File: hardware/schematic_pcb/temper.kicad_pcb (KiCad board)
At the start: 2 copper layers, 36 x 96.5 mm, 48 parts, among them J1 conn_01x03, J2 conn_01x03, J3 conn_01x03, J4 conn_01x03, J5 Charge Connector, J6 MCU Serial I/F, J7 Conn_01x08, M1 DMP3099L-7, Q1 2N7002, SW1 Reset, SW2 Factory Reset, SW3 ON/OFF, U1 MCP9700, U2 ESP32-WROOM-32, U3 APX803-31SAG-7

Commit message: Add 1.5 HW design.
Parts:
- removed MH1, MH2, MH3, MH4: MountingHole_3.2mm_M3, MountingHole:MountingHole_3.2mm_M3
- removed U3: APX803-31SAG-7, Package_TO_SOT_SMD:SOT-23
- added H1: MountingHole_3.2mm_M3, MountingHole:MountingHole_3.2mm_M3, F.Cu at (134.0, 56.8)
- added H2: MountingHole_3.2mm_M3, MountingHole:MountingHole_3.2mm_M3, F.Cu at (156.0, 56.8)
- added H3: MountingHole_3.2mm_M3, MountingHole:MountingHole_3.2mm_M3, F.Cu at (162.0, 145.2)
- added H4: MountingHole_3.2mm_M3, MountingHole:MountingHole_3.2mm_M3, F.Cu at (134.0, 145.2)
- added JP2: Jumper_2_Bridged, Jumper:SolderJumper-2_P1.3mm_Bridged_RoundedPad1.0x1.5mm, F.Cu at (132.8, 137.3)
- added Q2: 2N7002, Package_TO_SOT_SMD:SOT-23-3, F.Cu at (154.0, 126.9)
- added R17: 100k, Resistor_SMD:R_0402_1005Metric_Pad0.72x0.64mm_HandSolder, F.Cu at (157.8, 126.7)
- C1, C3, C4, C5: footprint Capacitor_SMD:C_0603_1608Metric -> Capacitor_SMD:C_0402_1005Metric_Pad0.74x0.62mm_HandSolder
- C2: value 0.1uf -> DNF; footprint Capacitor_SMD:C_0603_1608Metric -> Capacitor_THT:CP_Radial_D6.3mm_P2.50mm
- C6: value 470uf -> 0.1uf; footprint Capacitor_THT:CP_Radial_D6.3mm_P2.50mm -> Capacitor_SMD:C_0402_1005Metric_Pad0.74x0.62mm_HandSolder
- C7: value 0.1uf -> 22uf; footprint Capacitor_SMD:C_0603_1608Metric -> Capacitor_SMD:C_1206_3216Metric_Pad1.33x1.80mm_HandSolder
- D1: value PWR LED -> Blue Bluetooth LED; footprint LED_SMD:LED_1206_3216Metric -> LED_SMD:LED_0805_2012Metric_Pad1.15x1.40mm_HandSolder
- D2: value Blue Bluetooth LED -> Green WiFi LED; footprint LED_SMD:LED_1206_3216Metric -> LED_SMD:LED_0805_2012Metric_Pad1.15x1.40mm_HandSolder
- D3: value Green WiFi LED -> Red Charging LED; footprint LED_SMD:LED_1206_3216Metric -> LED_SMD:LED_0805_2012Metric_Pad1.15x1.40mm_HandSolder
- D4: value Red Charging LED -> PWR LED; footprint LED_SMD:LED_1206_3216Metric -> LED_SMD:LED_0805_2012Metric_Pad1.15x1.40mm_HandSolder
- J7: value Conn_01x08 -> Conn_01x10; footprint Connector_PinHeader_2.54mm:PinHeader_1x08_P2.54mm_Vertical -> Connector_PinHeader_2.54mm:PinHeader_1x10_P2.54mm_Vertical
- M1: value DMP3099L-7 -> AO3401A
- R1, R14, R2, R3, R4, R5, R8: footprint Resistor_SMD:R_0603_1608Metric_Pad0.98x0.95mm_HandSolder -> Resistor_SMD:R_0402_1005Metric_Pad0.72x0.64mm_HandSolder
- R10: value DNF -> 100k; footprint Resistor_SMD:R_0603_1608Metric_Pad0.98x0.95mm_HandSolder -> Resistor_SMD:R_0402_1005Metric_Pad0.72x0.64mm_HandSolder
- R11: value 150k -> 22k; footprint Resistor_SMD:R_0603_1608Metric_Pad0.98x0.95mm_HandSolder -> Resistor_SMD:R_0402_1005Metric_Pad0.72x0.64mm_HandSolder
- R12: value 47k -> 470R; footprint Resistor_SMD:R_0603_1608Metric_Pad0.98x0.95mm_HandSolder -> Resistor_SMD:R_0402_1005Metric_Pad0.72x0.64mm_HandSolder
- R13: value 470R -> 100k; footprint Resistor_SMD:R_0603_1608Metric_Pad0.98x0.95mm_HandSolder -> Resistor_SMD:R_0402_1005Metric_Pad0.72x0.64mm_HandSolder
- R15: value 150k -> 47k; footprint Resistor_SMD:R_0603_1608Metric_Pad0.98x0.95mm_HandSolder -> Resistor_SMD:R_0402_1005Metric_Pad0.72x0.64mm_HandSolder
- R16: value 68k -> 470R; footprint Resistor_SMD:R_0603_1608Metric_Pad0.98x0.95mm_HandSolder -> Resistor_SMD:R_0402_1005Metric_Pad0.72x0.64mm_HandSolder
- R6: value 470R -> 10k; footprint Resistor_SMD:R_0603_1608Metric_Pad0.98x0.95mm_HandSolder -> Resistor_SMD:R_0402_1005Metric_Pad0.72x0.64mm_HandSolder
- R7: value 10k -> 470R; footprint Resistor_SMD:R_0603_1608Metric_Pad0.98x0.95mm_HandSolder -> Resistor_SMD:R_0402_1005Metric_Pad0.72x0.64mm_HandSolder
- R9: value 470R -> DNF; footprint Resistor_SMD:R_0603_1608Metric_Pad0.98x0.95mm_HandSolder -> Resistor_SMD:R_0402_1005Metric_Pad0.72x0.64mm_HandSolder
- SW1: value Reset -> ON/OFF; footprint PJA_Switches:switch_SPST_5mmx3mmx2.5mm -> Button_Switch_SMD:SW_SPST_SKQG_WithoutStem
- SW2: value Factory Reset -> ON/OFF; footprint PJA_Switches:switch_SPST_5mmx3mmx2.5mm -> Button_Switch_SMD:SW_SPST_SKQG_WithoutStem
- SW3: footprint PJA_Switches:switch_SPST_5mmx3mmx2.5mm -> Button_Switch_SMD:SW_SPST_SKQG_WithoutStem
- moved C3 70.8 mm to (143.2, 139.0)
- moved D4 69.0 mm to (148.0, 133.5), turned to 0 degrees
- moved C7 66.8 mm to (156.4, 63.0), turned to 0 degrees
- moved R4 61.3 mm to (155.2, 66.0), turned to 180 degrees
- moved D1 42.5 mm to (138.7, 92.0), turned to -90 degrees
- moved R16 37.4 mm to (147.5, 131.8), turned to 0 degrees
- moved C4 35.5 mm to (157.9, 66.0), turned to 0 degrees
- moved R9 33.6 mm to (141.2, 101.5), turned to 90 degrees
- moved R8 32.9 mm to (152.2, 62.0), turned to 0 degrees
- moved R12 32.6 mm to (141.0, 65.7), turned to 90 degrees
- moved R6 32.6 mm to (141.2, 98.9), turned to 90 degrees
- moved R13 31.7 mm to (141.2, 96.2)
- moved R15 17.8 mm to (138.8, 111.2), turned to 0 degrees
- moved J7 17.5 mm to (157.5, 91.0)
- moved C1 15.6 mm to (150.5, 126.1), turned to -90 degrees
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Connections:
- net Net-(J7-Pin_5) renamed /PWR_SW_A
- net Net-(J7-Pin_6) renamed /PWR_SW_B
- C2 pad 1: //RESET -> 3v3
- C3 pad 1: 3v3 -> //RESET
- C4 pad 1: Net-(U2-IO34) -> 3v3
- C4 pad 2: Net-(Q1-D) -> GND
- C5 pad 1: Net-(U2-IO35) -> Net-(U2-IO34)
- C6 pad 1: 3v3 -> Net-(U2-IO35)
- C6 pad 2: GND -> Net-(Q1-D)
- D1 pad 2: 3v3 -> Net-(D1-A)
- D3 pad 1: Net-(D3-K) -> /CHRG_STAT
- D4 pad 2: Net-(D4-A) -> 3v3
- J6 pad 2: /TXD -> Net-(J6-Pin_2)
- J7 pad 7: Net-(D4-K) -> /CHRG_STAT
- JP1 pad 2: /TXD -> Net-(J6-Pin_2)
- R10 pad 1: Net-(Q1-D) -> /+VBAT
- R10 pad 2: GND -> Net-(U2-IO34)
- R11 pad 1: /+VBAT -> Net-(U2-IO34)
- R11 pad 2: Net-(U2-IO34) -> Net-(Q1-D)
- R12 pad 1: Net-(U2-IO34) -> /+VBAT
- R12 pad 2: Net-(Q1-D) -> Net-(D3-A)
- R13 pad 1: /+VBAT -> Net-(Q1-G)
- R13 pad 2: Net-(D4-A) -> GND
- R14 pad 1: Net-(Q1-G) -> 3v3
- R14 pad 2: GND -> Net-(U2-IO35)
- R15 pad 1: 3v3 -> Net-(U2-IO35)
- R15 pad 2: Net-(U2-IO35) -> Net-(Q1-D)
- R16 pad 1: Net-(U2-IO35) -> Net-(D4-K)
- R16 pad 2: Net-(Q1-D) -> Net-(Q2-D)
- R6 pad 1: Net-(D1-K) -> 3v3
- R6 pad 2: GND -> Net-(SW2-B)
- R7 pad 1: 3v3 -> Net-(D1-K)
- R7 pad 2: Net-(SW2-B) -> GND
- R9 pad 1: Net-(D3-K) -> Net-(Q1-D)
- U2 pad 24: Net-(D3-A) -> Net-(D2-A)
- U2 pad 26: Net-(D2-A) -> Net-(D1-A)
- U2 pad 33: unconnected-(U2-IO21-Pad33) -> //CHRG_OFF
- U2 pad 36: unconnected-(U2-IO22-Pad36) -> //DIS_PWR_LED
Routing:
- net Net-(D4-K): track 91.4 -> 1.77 mm
- net /CHRG_STAT: track 0.00 -> 57.3 mm, vias 0 -> 1
- net //DIS_PWR_LED: track 0.00 -> 47.1 mm, vias 0 -> 4
- net //CHRG_OFF: track 0.00 -> 41.4 mm, vias 0 -> 2
- net /PWR_SW_B: track 29.1 -> 66.4 mm, vias 1 -> 2
- net Net-(D2-K): track 36.7 -> 1.93 mm, vias 2 -> 0
- net Net-(D3-A): track 36.4 -> 2.29 mm, vias 2 -> 0
- net //RESET: track 79.1 -> 112.0 mm, vias 2 -> 1
- net Net-(J1-Pin_3): track 73.1 -> 103.4 mm
- net Net-(D1-A): track 0.00 -> 22.9 mm, vias 0 -> 4
- net Net-(U2-IO35): track 37.1 -> 59.8 mm
- net Net-(J6-Pin_2): track 0.00 -> 21.8 mm, vias 0 -> 1
- net /PWR_SW_A: track 43.2 -> 63.1 mm, vias 1 -> 0
- net /TXD: track 98.6 -> 80.4 mm, vias 1 -> 4
- net Net-(Q1-G): track 47.9 -> 30.6 mm
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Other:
- board text added: "ON OFF"
- board text added: "TEMPER V1.5 ASY0400V1.5"
- board text removed: "ON / OFF"
- board text removed: "TEMPER V1.4 ASY0400V1.4"

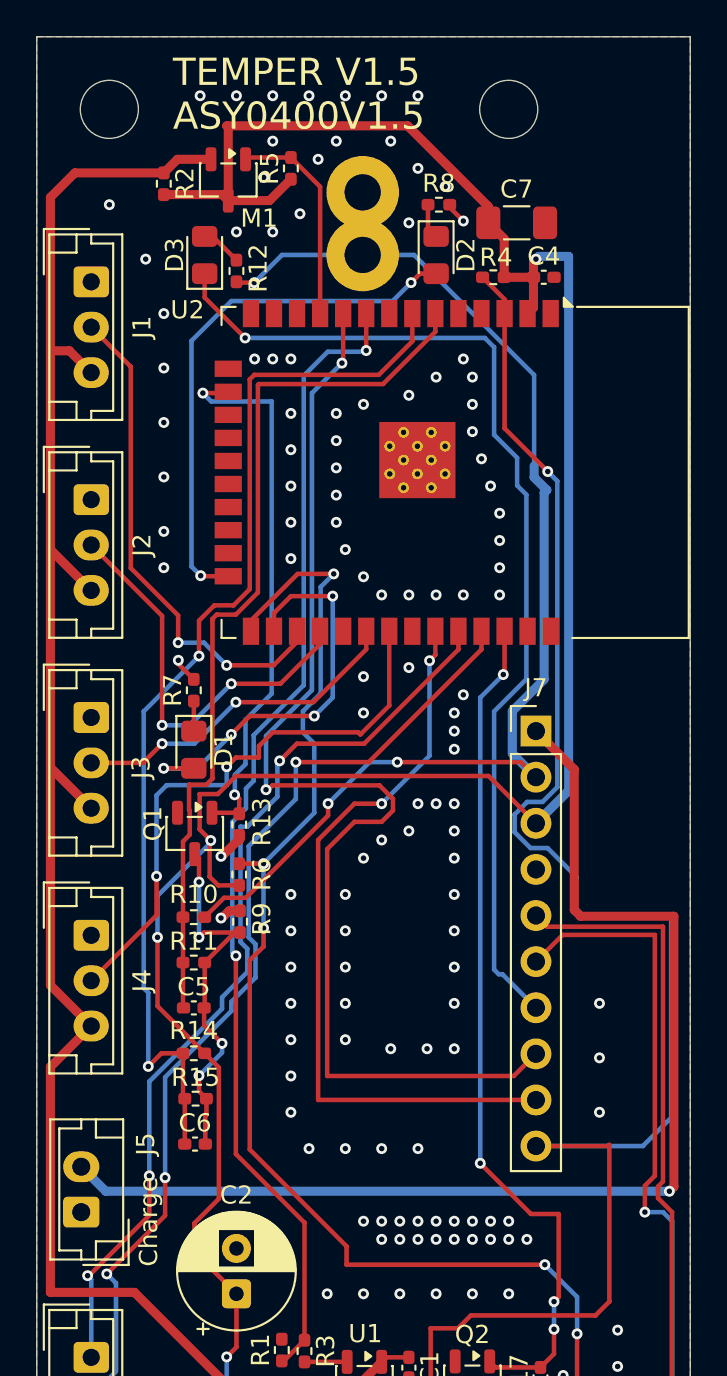
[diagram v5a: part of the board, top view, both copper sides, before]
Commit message: Update to add D5.
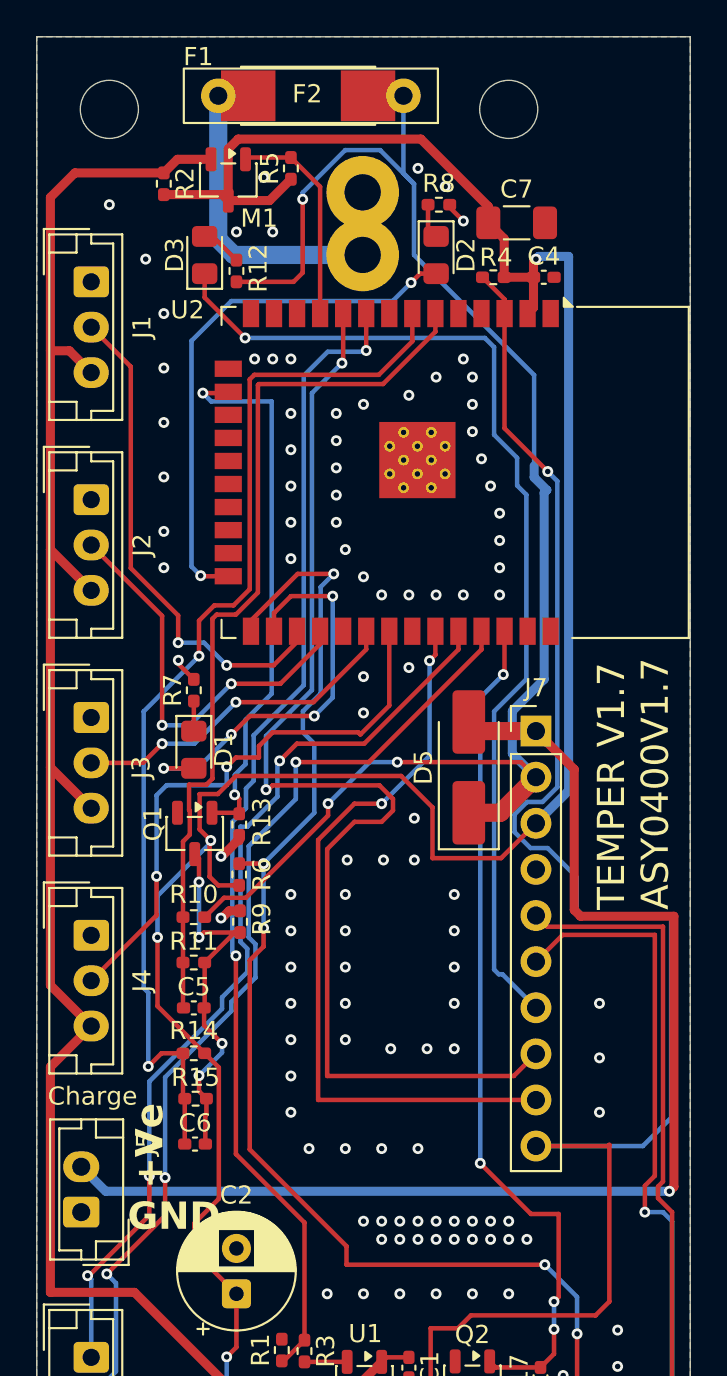
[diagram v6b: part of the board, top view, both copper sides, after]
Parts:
- added D5: 1N5819, Diode_SMD:D_SMA_Handsoldering, F.Cu at (153.8, 93.0)
- added F1: 3A, PJA_Fuses:PTC_23mm_3mm_10.2mm_wire_spacing, F.Cu at (145.1, 56.0)
- added F2: DNF, PJA_Fuses:Scherter_OMT125, F.Cu at (144.9, 56.0)
- D2: value Green WiFi LED -> GreenLED
- D4: value PWR LED -> GreenLED
- SW1, SW2, SW3: value ON/OFF -> tactsw
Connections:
- BT1 pad 1: /+VBAT -> Net-(BT1-+)
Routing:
- net /+VBAT: track 66.1 -> 85.4 mm
- net Net-(BT1-+): track 0.00 -> 16.2 mm
- net +5v: track 64.6 -> 68.5 mm
- net 3v3: track 158.6 -> 160.4 mm
- net GND: vias 139 -> 118
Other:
- board text added: "+Ve"
- board text added: "GND"
- board text added: "TEMPER V1.7 ASY0400V1.7"
- board text removed: "TEMPER V1.5 ASY0400V1.5"
